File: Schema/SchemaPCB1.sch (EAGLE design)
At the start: 30 parts, among them J1 CON-HIROSE-COAXIAL-U.FL, J2 Programmer, U1 RN2483, U2 TPS22860DBVR, U3 ESP32, U4 SOT-89-5, U5 SI7217-B-01-IVR

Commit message: Eagle fix
Board bijna klaar
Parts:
- removed Q?1: PMOS, gps:PMOS
- removed R4, R5, R8: (no value), rcl:R-EU_R0805
- added C11, C13: (no value), rcl:C-EUC0805
- added U6: TPS22860DBVR, --CoolTeamLib:TPS22860DBVR
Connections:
- removed net *GPS_ENABLE: Q?1.G, R8.2, U3.NC_7
- removed net N$1: U3.GND_10, U3.GND_11, U3.GND_12, U3.GND_3, U3.GND_4, U3.GND_5, U3.GND_6, U3.GND_7, U3.GND_8, U3.GND_9
- removed net N$2: J3.1
- removed net N$3: J3.2
- removed net N$5: R4.1, U?1.WAKE-UP
- removed net N$8: C10.1, C12.1, L1.1, R5.2, U?1.VCC
- new net IO1: J3.3, U3.NC_6
- new net IO2: J3.2, U3.IO15
- new net IO3: J3.1, U3.IO2
- net +3V3: now also C13.1, U6.VBIAS, U6.VIN; no longer Q?1.S1, Q?1.S2, Q?1.S3
- net GND: now also C11.2, C13.2, U3.GND_10, U3.GND_11, U3.GND_12, U3.GND_3, U3.GND_4, U3.GND_5, U3.GND_6, U3.GND_7, U3.GND_8, U3.GND_9, U6.GND, U?1.WAKE-UP; no longer R4.2
- net GPS_ENABLE: now also U3.NC_7, U6.ON; no longer R8.1
- net HALL_DATA: no longer J3.3
- net N$6: now also C10.1, C12.1, L1.1, U?1.VCC; no longer R5.1
- net N$7: now also C11.1, U6.VOUT; no longer Q?1.D1, Q?1.D2, Q?1.D3, Q?1.D4
- net RXD0: now also J3.5; no longer J3.6
- net TXD0: now also J3.6; no longer J3.5

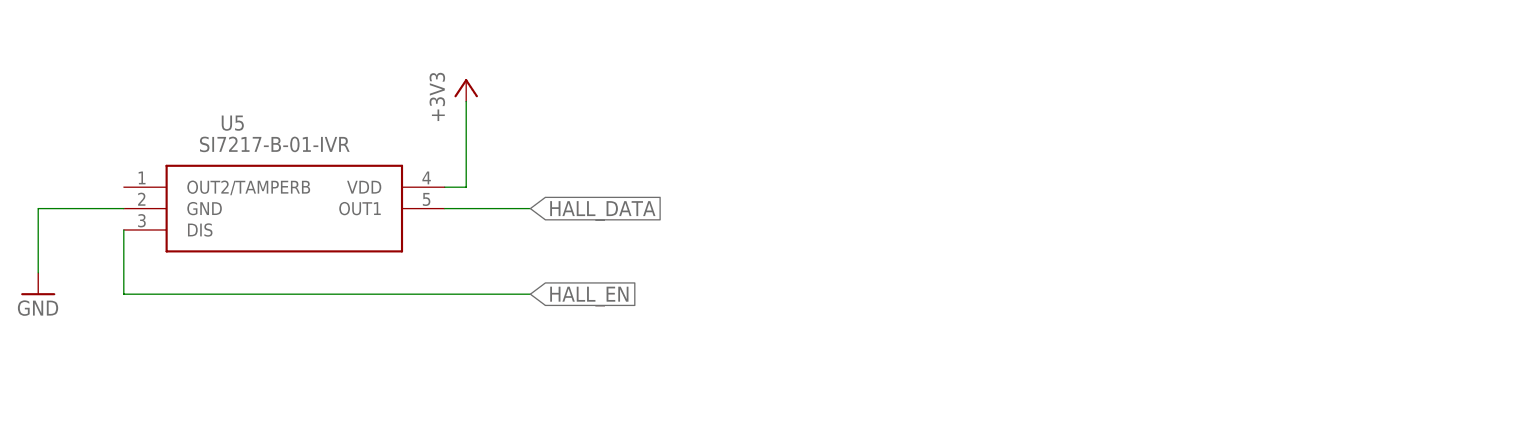
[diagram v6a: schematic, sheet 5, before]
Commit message: laatste componenten en pcb2 toegevoegd
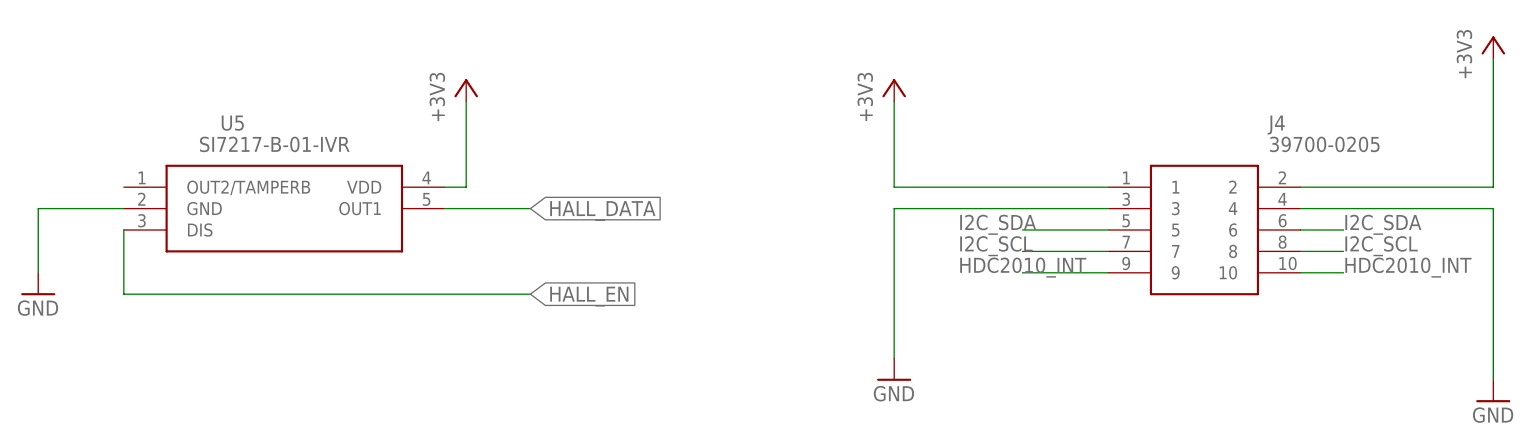
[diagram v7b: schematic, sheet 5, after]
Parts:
- added J4: 39700-0205, --CoolTeamLib:39700-0205
- added J5: 39700-0002, --CoolTeamLib:39700-0002
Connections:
- new net HDC2010_INT: J4.10, J4.9, U3.IO25
- net +3V3: now also J4.1, J4.2
- net BAT_IN: now also J5.2, J5.4
- net GND: now also J4.3, J4.4, J5.1, J5.3
- net I2C_SCL: now also J4.7, J4.8
- net I2C_SDA: now also J4.5, J4.6
- net IO1: now also U3.IO14; no longer U3.NC_6
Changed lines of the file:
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@@
 <drawing>
 <settings>
-<setting alwaysvectorfont="no"/>
+<setting alwaysvectorfont="yes"/>
 <setting keepoldvectorfont="yes"/>
 <setting verticaltext="up"/>
@@
 <part name="+3V2" library="supply1" library_urn="urn:adsk.eagle:library:371" deviceset="+3V3" device=""/>
 <part name="GND19" library="supply1" library_urn="urn:adsk.eagle:library:371" deviceset="GND" device=""/>
+<part name="J4" library="--CoolTeamLib" deviceset="39700-0205" device=""/>
+<part name="GND20" library="supply1" library_urn="urn:adsk.eagle:library:371" deviceset="GND" device=""/>
+<part name="+3V8" library="supply1" library_urn="urn:adsk.eagle:library:371" deviceset="+3V3" device=""/>
+<part name="GND21" library="supply1" library_urn="urn:adsk.eagle:library:371" deviceset="GND" device=""/>
+<part name="+3V11" library="supply1" library_urn="urn:adsk.eagle:library:371" deviceset="+3V3" device=""/>
+<part name="J5" library="--CoolTeamLib" deviceset="39700-0002" device=""/>
+<part name="GND22" library="supply1" library_urn="urn:adsk.eagle:library:371" deviceset="GND" device=""/>
 </parts>
 <sheets>
@@
 </segment>
 <segment>
-<pinref part="U3" gate="G$1" pin="NC_6"/>
-<wire x1="127" y1="78.74" x2="116.84" y2="78.74" width="0.1524" layer="91"/>
-<label x="116.84" y="78.74" size="1.778" layer="95"/>
+<pinref part="U3" gate="G$1" pin="IO14"/>
+<wire x1="127" y1="101.6" x2="116.84" y2="101.6" width="0.1524" layer="91"/>
+<label x="116.84" y="101.6" size="1.778" layer="95"/>
 </segment>
 </net>
@@
 <wire x1="127" y1="73.66" x2="116.84" y2="73.66" width="0.1524" layer="91"/>
 <label x="116.84" y="73.66" size="1.778" layer="95"/>
+</segment>
+</net>
+<net name="HDC2010_INT" class="0">
+<segment>
+<pinref part="U3" gate="G$1" pin="IO25"/>
+<wire x1="127" y1="109.22" x2="114.3" y2="109.22" width="0.1524" layer="91"/>
+<label x="114.3" y="109.22" size="1.778" layer="95" rot="R180" xref="yes"/>
 </segment>
 </net>
@@
 <segment>
 <wire x1="93.98" y1="132.08" x2="86.36" y2="132.08" width="0.1524" layer="91"/>
-<label x="81.28" y="132.08" size="1.778" layer="95" rot="R180"/>
 <pinref part="U?1" gate="G$1" pin="I2C_SDA"/>
 <pinref part="R7" gate="G$1" pin="1"/>
@@
 <segment>
 <wire x1="93.98" y1="127" x2="78.74" y2="127" width="0.1524" layer="91"/>
-<label x="73.66" y="127" size="1.778" layer="95" rot="R180"/>
 <pinref part="U?1" gate="G$1" pin="I2C_SCL"/>
 <wire x1="78.74" y1="132.08" x2="78.74" y2="127" width="0.1524" layer="91"/>
@@
 <attribute name="VALUE" x="157.48" y="104.14" size="1.778" layer="96"/>
 </instance>
+<instance part="J5" gate="G$1" x="63.5" y="170.18" smashed="yes">
+<attribute name="NAME" x="69.85" y="177.8" size="1.778" layer="95" align="center-left"/>
+<attribute name="VALUE" x="69.85" y="175.26" size="1.778" layer="96" align="center-left"/>
+</instance>
+<instance part="GND22" gate="1" x="60.96" y="160.02" smashed="yes">
+<attribute name="VALUE" x="58.42" y="157.48" size="1.778" layer="96"/>
+</instance>
 </instances>
 <busses>
@@
 <pinref part="GND4" gate="1" pin="GND"/>
 </segment>
+<segment>
+<pinref part="J5" gate="G$1" pin="1"/>
+<wire x1="63.5" y1="167.64" x2="60.96" y2="167.64" width="0.1524" layer="91"/>
+<wire x1="60.96" y1="167.64" x2="60.96" y2="162.56" width="0.1524" layer="91"/>
+<wire x1="60.96" y1="162.56" x2="86.36" y2="162.56" width="0.1524" layer="91"/>
+<wire x1="86.36" y1="162.56" x2="86.36" y2="167.64" width="0.1524" layer="91"/>
+<pinref part="J5" gate="G$1" pin="3"/>
+<wire x1="86.36" y1="167.64" x2="83.82" y2="167.64" width="0.1524" layer="91"/>
+<pinref part="GND22" gate="1" pin="GND"/>
+<junction x="60.96" y="162.56"/>
+</segment>
 </net>
 <net name="BAT_IN" class="0">
@@
 <junction x="99.06" y="127"/>
 <label x="71.12" y="127" size="1.778" layer="95" rot="R180" xref="yes"/>
+</segment>
+<segment>
+<pinref part="J5" gate="G$1" pin="4"/>
+<wire x1="83.82" y1="170.18" x2="93.98" y2="170.18" width="0.1524" layer="91"/>
+<label x="93.98" y="170.18" size="1.778" layer="95" xref="yes"/>
+</segment>
+<segment>
+<pinref part="J5" gate="G$1" pin="2"/>
+<wire x1="63.5" y1="170.18" x2="53.34" y2="170.18" width="0.1524" layer="91"/>
+<label x="53.34" y="170.18" size="1.778" layer="95"/>
 </segment>
 </net>
@@
 <attribute name="DRAWING_NAME" x="190.5" y="19.05" size="2.54" layer="94"/>
 </instance>
+<instance part="J4" gate="G$1" x="195.58" y="104.14" smashed="yes">
+<attribute name="NAME" x="214.63" y="111.76" size="1.778" layer="95" align="center-left"/>
+<attribute name="VALUE" x="214.63" y="109.22" size="1.778" layer="96" align="center-left"/>
+</instance>
+<instance part="GND20" gate="1" x="241.3" y="78.74" smashed="yes">
+<attribute name="VALUE" x="238.76" y="76.2" size="1.778" layer="96"/>
+</instance>
+<instance part="+3V8" gate="G$1" x="241.3" y="121.92" smashed="yes">
+<attribute name="VALUE" x="238.76" y="116.84" size="1.778" layer="96" rot="R90"/>
+</instance>
+<instance part="GND21" gate="1" x="170.18" y="81.28" smashed="yes">
+<attribute name="VALUE" x="167.64" y="78.74" size="1.778" layer="96"/>
+</instance>
+<instance part="+3V11" gate="G$1" x="170.18" y="116.84" smashed="yes">
+<attribute name="VALUE" x="167.64" y="111.76" size="1.778" layer="96" rot="R90"/>
+</instance>
 </instances>
 <busses>
@@
 <wire x1="119.38" y1="104.14" x2="116.84" y2="104.14" width="0.1524" layer="91"/>
 </segment>
+<segment>
+<pinref part="J4" gate="G$1" pin="2"/>
+<wire x1="218.44" y1="104.14" x2="241.3" y2="104.14" width="0.1524" layer="91"/>
+<wire x1="241.3" y1="104.14" x2="241.3" y2="119.38" width="0.1524" layer="91"/>
+<pinref part="+3V8" gate="G$1" pin="+3V3"/>
+</segment>
+<segment>
+<pinref part="J4" gate="G$1" pin="1"/>
+<wire x1="195.58" y1="104.14" x2="170.18" y2="104.14" width="0.1524" layer="91"/>
+<wire x1="170.18" y1="104.14" x2="170.18" y2="114.3" width="0.1524" layer="91"/>
+<pinref part="+3V11" gate="G$1" pin="+3V3"/>
+</segment>
 </net>
 <net name="GND" class="0">
@@
 <wire x1="68.58" y1="101.6" x2="78.74" y2="101.6" width="0.1524" layer="91"/>
 </segment>
+<segment>
+<pinref part="J4" gate="G$1" pin="4"/>
+<wire x1="218.44" y1="101.6" x2="241.3" y2="101.6" width="0.1524" layer="91"/>
+<wire x1="241.3" y1="101.6" x2="241.3" y2="81.28" width="0.1524" layer="91"/>
+<pinref part="GND20" gate="1" pin="GND"/>
+</segment>
+<segment>
+<pinref part="J4" gate="G$1" pin="3"/>
+<wire x1="195.58" y1="101.6" x2="170.18" y2="101.6" width="0.1524" layer="91"/>
+<wire x1="170.18" y1="101.6" x2="170.18" y2="83.82" width="0.1524" layer="91"/>
+<pinref part="GND21" gate="1" pin="GND"/>
+</segment>
 </net>
 <net name="HALL_EN" class="0">
@@
 </segment>
 </net>
+<net name="I2C_SDA" class="0">
+<segment>
+<pinref part="J4" gate="G$1" pin="6"/>
+<wire x1="218.44" y1="99.06" x2="223.52" y2="99.06" width="0.1524" layer="91"/>
+<label x="223.52" y="99.06" size="1.778" layer="95"/>
+</segment>
+<segment>
+<pinref part="J4" gate="G$1" pin="5"/>
+<wire x1="195.58" y1="99.06" x2="185.42" y2="99.06" width="0.1524" layer="91"/>
+<label x="177.8" y="99.06" size="1.778" layer="95"/>
+</segment>
+</net>
+<net name="I2C_SCL" class="0">
+<segment>
+<pinref part="J4" gate="G$1" pin="8"/>
+<wire x1="218.44" y1="96.52" x2="223.52" y2="96.52" width="0.1524" layer="91"/>
+<label x="223.52" y="96.52" size="1.778" layer="95"/>
+</segment>
+<segment>
+<pinref part="J4" gate="G$1" pin="7"/>
+<wire x1="195.58" y1="96.52" x2="185.42" y2="96.52" width="0.1524" layer="91"/>
+<label x="177.8" y="96.52" size="1.778" layer="95"/>
+</segment>
+</net>
+<net name="HDC2010_INT" class="0">
+<segment>
+<pinref part="J4" gate="G$1" pin="10"/>
+<wire x1="218.44" y1="93.98" x2="223.52" y2="93.98" width="0.1524" layer="91"/>
+<label x="223.52" y="93.98" size="1.778" layer="95"/>
+</segment>
+<segment>
+<pinref part="J4" gate="G$1" pin="9"/>
+<wire x1="195.58" y1="93.98" x2="185.42" y2="93.98" width="0.1524" layer="91"/>
+<label x="177.8" y="93.98" size="1.778" layer="95"/>
+</segment>
+</net>
